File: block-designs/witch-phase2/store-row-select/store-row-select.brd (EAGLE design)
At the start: 27.9 x 27.9 mm, 11 parts, among them IC1 74LVC1G18DBVR, IC2 74AHC1G32DBV, IC3 74LVC1G08DBV

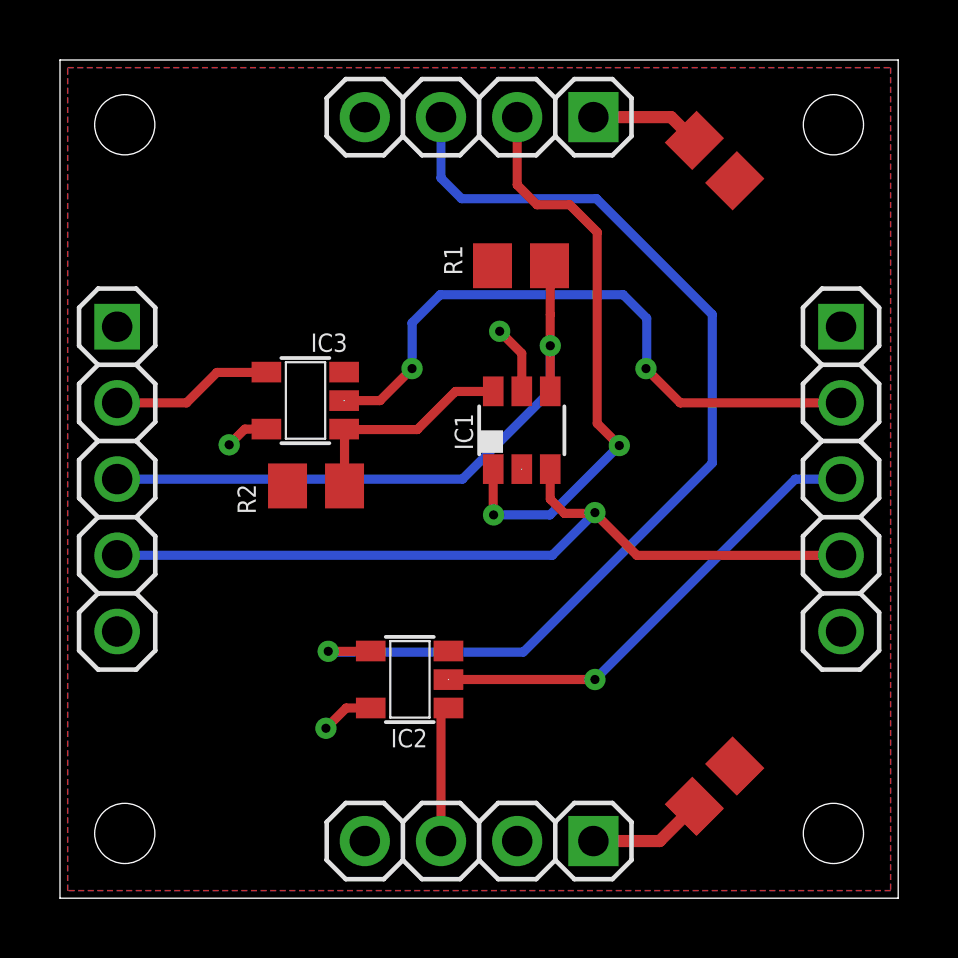
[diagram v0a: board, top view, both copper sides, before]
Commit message: updated designs for new labeling and spacing
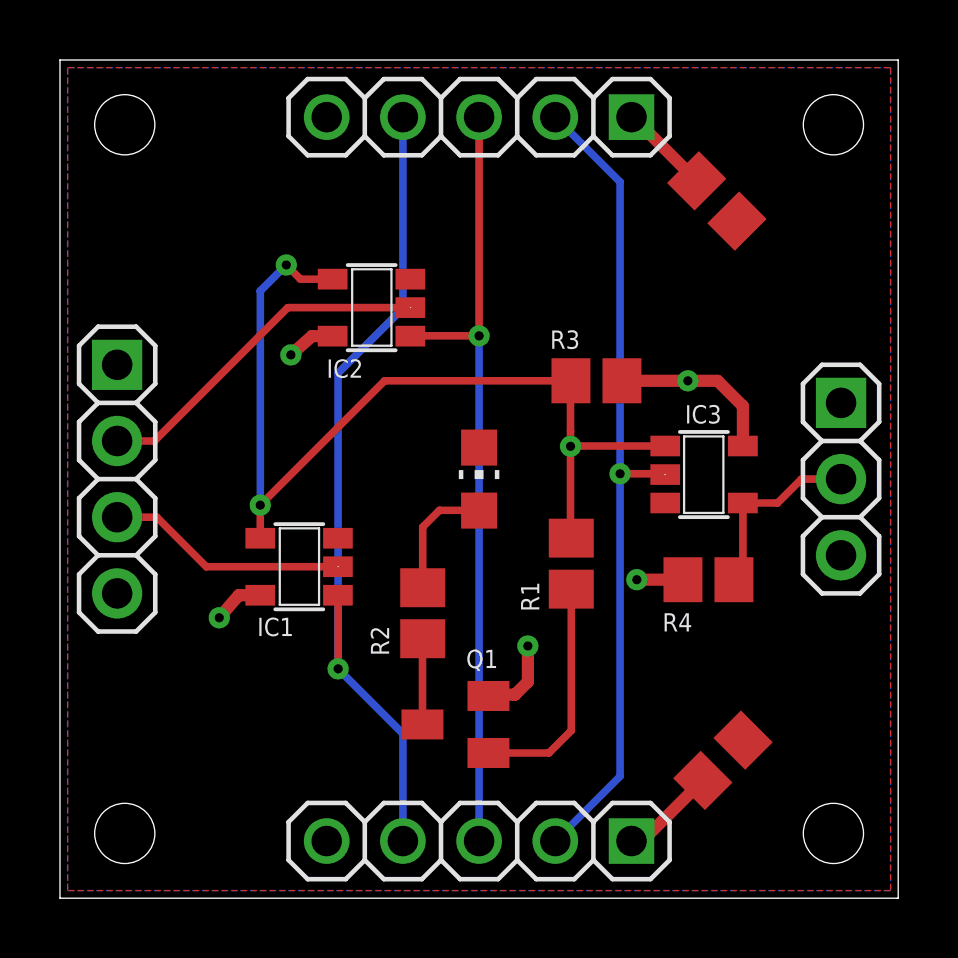
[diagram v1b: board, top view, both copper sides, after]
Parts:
- added LED1: (no value), led:CHIP-LED0805
- added Q1: MMBT2907ALT1SMD, transistor-pnp:SOT23-BEC
- added R3, R4: (no value), resistor:R0805
- IC1: value 74LVC1G18DBVR -> 74LVC1G125DBV; device 74xx-little-us:DBV_R-PDSO-G6 -> 74xx-little-us:SOT23-5
- IC2: value 74AHC1G32DBV -> 74LVC1G125DBV
- IC3: value 74LVC1G08DBV -> 74LVC1G125DBV
- JP3: device pinhead:1X04 -> pinhead:1X05
- JP4: device pinhead:1X05 -> pinhead:1X03
- moved JP3 24.1 mm to (14.0, 26.0)
- moved C2 20.0 mm to (22.1, 4.60), turned to 45 degrees
- moved C1 19.5 mm to (21.9, 23.2), turned to 315 degrees
- moved JP2 17.1 mm to (14.0, 1.91), turned to 180 degrees
- moved JP1 17.1 mm to (1.91, 14.0), turned to 270 degrees
- moved IC3 13.5 mm to (21.5, 14.1), turned to 270 degrees
- moved IC2 12.5 mm to (10.4, 19.7)
- moved R1 10.1 mm to (17.0, 11.2), turned to 90 degrees
- moved IC1 8.70 mm to (7.98, 11.0), turned to 90 degrees
- moved R2 5.54 mm to (12.1, 9.50), turned to 90 degrees
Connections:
- removed net CARRY_DONE: IC1.6, IC3.1, R2.1
- removed net CARRY_EN: IC1.1, JP1.2
- removed net CARRY_IN: IC2.2, JP4.3
- removed net CARRY_NEXT: IC3.4, JP2.2
- removed net CARRY_OUT: IC1.4, JP2.3, R1.1
- removed net CARRY_PREV: IC3.2, JP4.2
- removed net CARRY_PULSE: IC1.3, JP2.4, JP4.4
- removed net CLK_IN: IC2.1, JP3.3
- removed net CLK_OUT: IC2.4, JP1.3
- new net ENABLE: IC1.4, IC2.4, IC3.1, R1.2, R3.1
- new net N$2: Q1.B, R1.1
- new net N$4: Q1.C, R2.1
- new net N$5: LED1.A, R2.2
- new net RCV_EN: IC1.1, JP2.4, JP3.4
- new net RCV_ROW: IC1.2, JP1.3
- new net ROW_EN: IC3.4, JP4.2, R4.1
- new net SND_EN: IC2.1, JP2.3, JP3.3
- new net SND_RCV: IC3.2, JP2.2, JP3.2
- new net SND_ROW: IC2.2, JP1.2
- net GND: now also IC1.3, JP3.5, JP4.3, LED1.C; no longer IC1.2, JP3.4, JP4.5, R1.2, R2.2
- net VCC: now also Q1.E, R3.2, R4.2
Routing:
- net CLK_OUT: track 34.8 -> 0.00 mm, vias 1 -> 0
- net ENABLE: track 0.00 -> 31.7 mm, vias 0 -> 3
- net RCV_EN: track 0.00 -> 28.5 mm, vias 0 -> 1
- net CARRY_PULSE: track 28.0 -> 0.00 mm, vias 1 -> 0
- net SND_RCV: track 0.00 -> 27.4 mm, vias 0 -> 1
- net SND_EN: track 0.00 -> 26.4 mm, vias 0 -> 1
- net CARRY_PREV: track 21.4 -> 0.00 mm, vias 2 -> 0
- net CARRY_OUT: track 21.4 -> 0.00 mm, vias 1 -> 0
- net CARRY_EN: track 19.7 -> 0.00 mm, vias 2 -> 0
- net CARRY_IN: track 15.9 -> 0.00 mm, vias 1 -> 0
- net SND_ROW: track 0.00 -> 11.6 mm
- net RCV_ROW: track 0.00 -> 8.04 mm
- net N$2: track 0.00 -> 7.78 mm
- net CARRY_DONE: track 7.39 -> 0.00 mm
- net VCC: track 13.1 -> 19.6 mm, vias 3 -> 5
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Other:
- board text added: "ROW SELECT"
- board text added: "SEL"
- board text removed: "CARRY SELECT"
